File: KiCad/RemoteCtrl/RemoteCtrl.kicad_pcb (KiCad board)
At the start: 2 copper layers, 91 parts, among them J1 UI, SW1 MX1A-E1NW, SW2 MX1A-E1NW, SW3 MX1A-E1NW, SW4 MX1A-E1NW, SW5 MX1A-E1NW, SW6 MX1A-E1NW, SW7 MX1A-E1NW, SW8 MX1A-E1NW, U1 74LVC1G17, U2 74LVC1G17, U3 74LVC1G17, U4 74LVC1G17, U5 74LVC1G17, U6 74LVC1G17, U7 74LVC1G17, U8 74LVC1G17

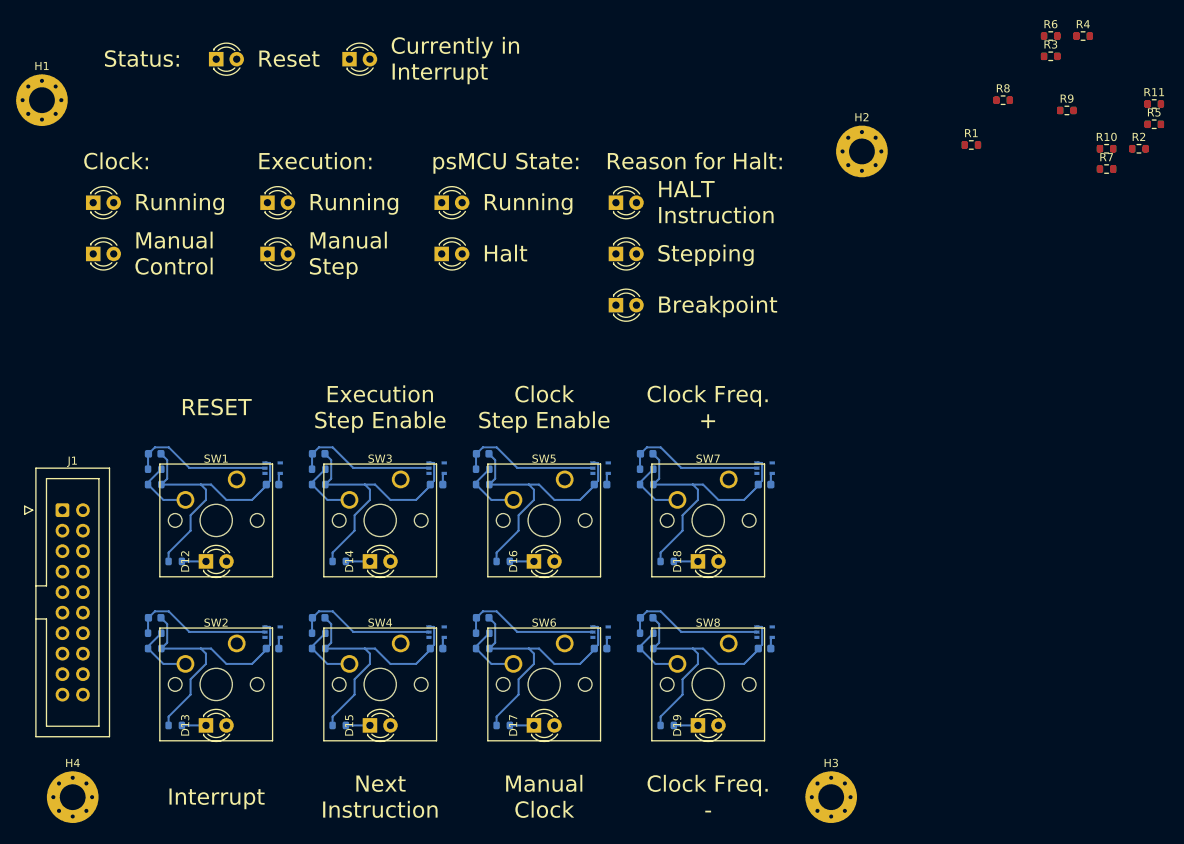
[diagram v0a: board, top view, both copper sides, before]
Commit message: Rough layout of Remote finished.
    Did not do connector yet, in case that changes with
    psMCU layout.
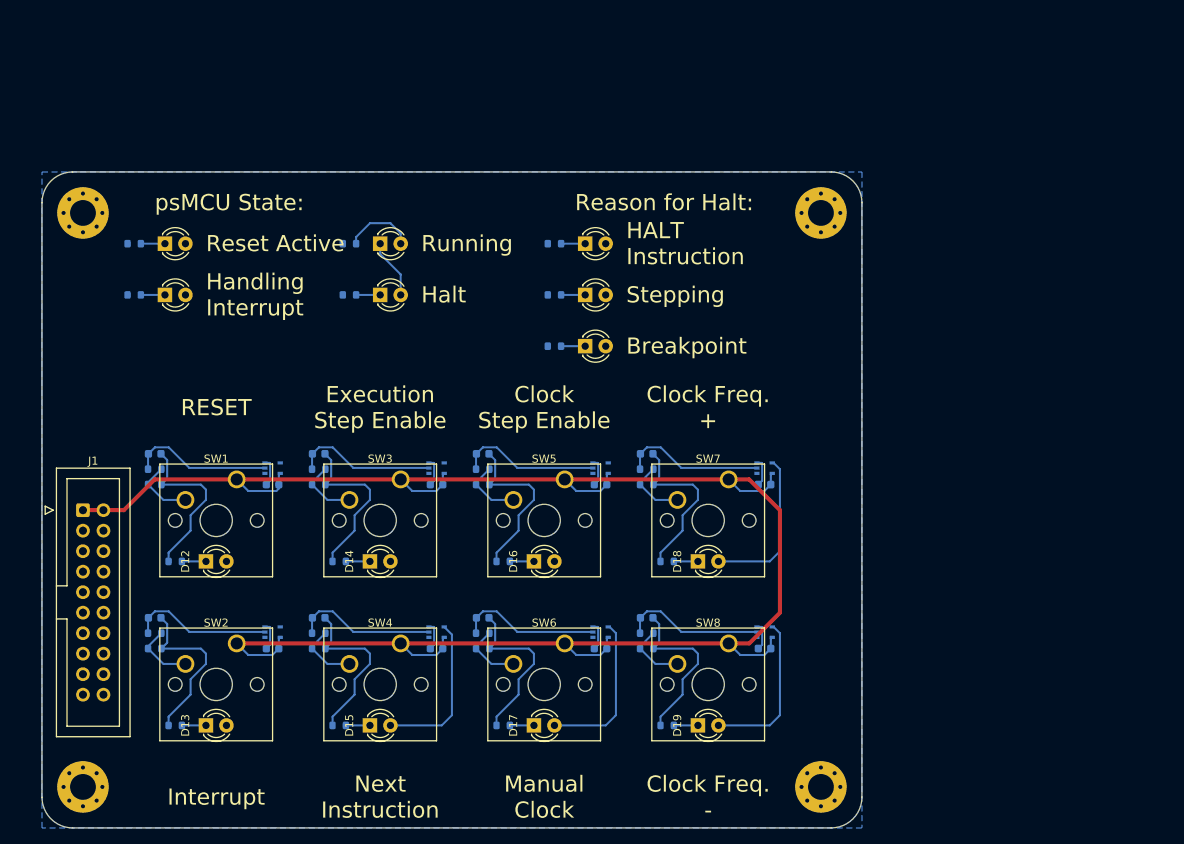
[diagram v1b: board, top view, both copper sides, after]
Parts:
- removed D3, D4, D5, D6: LED, LED_THT:LED_D3.0mm
- removed R3, R4, R5, R6: rled, Resistor_SMD:R_0603_1608Metric
- R1, R10, R11, R2, R7, R8, R9: moved to B.Cu
- moved R2 125.8 mm to (104.1, 43.2), turned to 180 degrees
- moved R1 104.4 mm to (104.1, 36.8), turned to 180 degrees
- moved R7 95.1 mm to (130.8, 43.2), turned to 180 degrees
- moved R8 82.9 mm to (130.8, 36.8), turned to 180 degrees
- moved R11 80.1 mm to (156.2, 49.5), turned to 180 degrees
- moved R10 70.8 mm to (156.2, 43.2), turned to 180 degrees
- moved R9 65.6 mm to (156.2, 36.8), turned to 180 degrees
- moved D2 37.1 mm to (108.0, 43.2)
- moved D1 23.7 mm to (108.0, 36.8)
- moved H1 14.9 mm to (97.8, 33.0)
- moved H2 9.16 mm to (189.2, 33.0)
- moved D7 9.16 mm to (134.6, 43.2)
- moved D8 9.16 mm to (134.6, 36.8)
- moved D10 6.35 mm to (160.0, 43.2)
- moved D11 6.35 mm to (160.0, 49.5)
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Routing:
- net +5V: track 11.7 -> 232.2 mm
- net GND: track 274.3 -> 196.1 mm
- net /BTN_INC_CLK_F: track 0.00 -> 19.6 mm
- net /BTN_DEC_CLK_F: track 0.00 -> 19.6 mm
- net /BTN_CLK_STEP: track 0.00 -> 19.6 mm
- net /BTN_INST_STEP: track 0.00 -> 19.5 mm
- net Net-(D8-Pad2): track 0.00 -> 8.86 mm
- net /LED_Halted: track 0.00 -> 7.40 mm
- net Net-(D9-Pad1): track 0.00 -> 2.99 mm
- net Net-(D7-Pad1): track 0.00 -> 2.99 mm
- net Net-(D11-Pad1): track 0.00 -> 2.99 mm
- net Net-(D10-Pad1): track 0.00 -> 2.99 mm
- net Net-(D2-Pad1): track 0.00 -> 2.98 mm
- net Net-(D1-Pad1): track 0.00 -> 2.98 mm
- added copper zone on B.Cu, net GND
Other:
- board outline added: 101.6 x 81.3 mm
- board text added: "Handling Interrupt"
- board text added: "Reset Active"
- board text removed: "Clock:"
- board text removed: "Currently in Interrupt"
- board text removed: "Execution:"
- board text removed: "Manual Control"
- board text removed: "Manual Step"
- board text removed: "Reset"
- board text removed: "Status:"

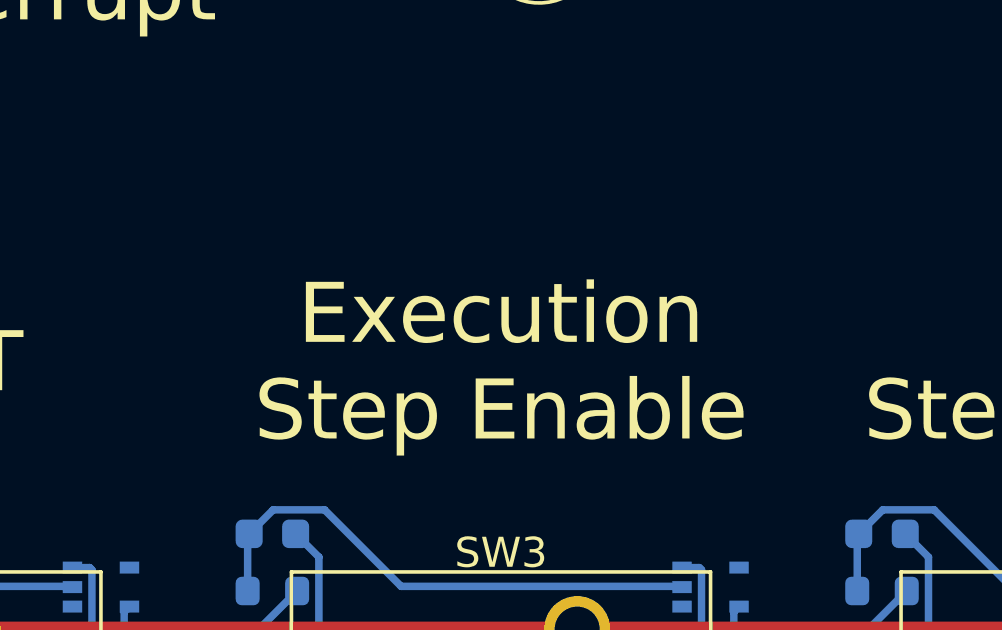
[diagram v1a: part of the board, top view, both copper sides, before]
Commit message: Worked on side-pcbs
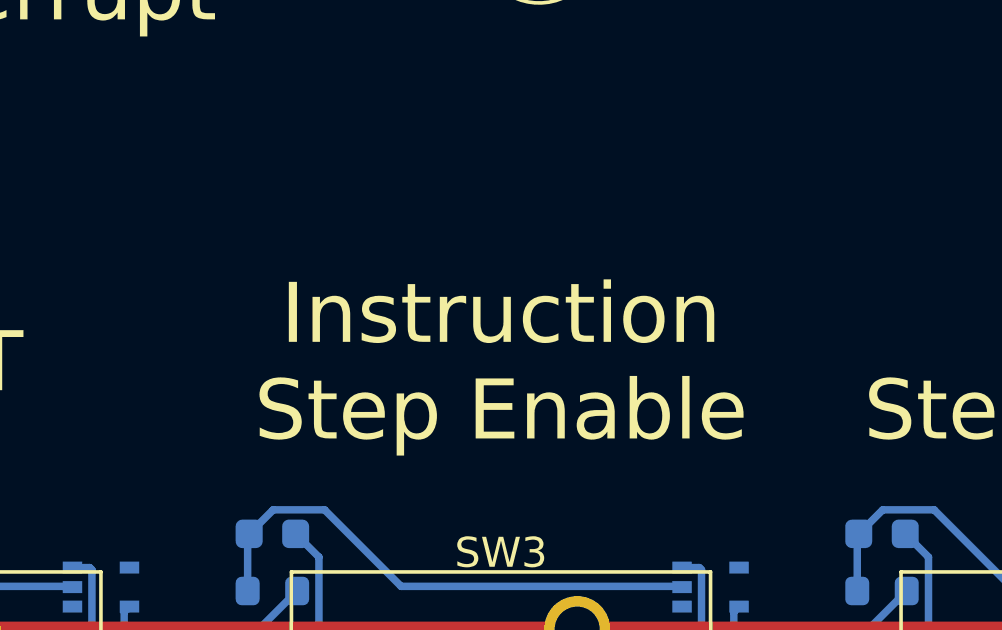
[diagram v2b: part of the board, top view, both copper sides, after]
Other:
- board text added: "Instruction Step Enable"
- board text removed: "Execution Step Enable"

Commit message: First draft Remote Control
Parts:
- moved J1 23.0 mm to (100.3, 92.7), turned to 180 degrees
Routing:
- net /LED_Halted_Inst: track 0.00 -> 109.2 mm, vias 0 -> 1
- net /BTN_INC_CLK_F: track 19.6 -> 124.6 mm, vias 0 -> 5
- net /LED_Halted_Step: track 0.00 -> 100.6 mm, vias 0 -> 1
- net /BTN_DEC_CLK_F: track 19.6 -> 108.3 mm
- net /LED_Halted_Bkpt: track 0.00 -> 88.0 mm, vias 0 -> 1
- net /BTN_CLK_STEP_EN: track 0.00 -> 82.8 mm, vias 0 -> 1
- net /LED_CLK_STEP_EN: track 0.00 -> 76.9 mm, vias 0 -> 5
- net /LED_INT_Active: track 0.00 -> 74.3 mm, vias 0 -> 4
- net /BTN_CLK_STEP: track 19.6 -> 90.2 mm, vias 0 -> 1
- net /LED_Halted: track 7.40 -> 74.6 mm, vias 0 -> 1
- net /RESET: track 0.00 -> 65.9 mm, vias 0 -> 3
- net /BTN_INST_STEP_EN: track 0.00 -> 62.5 mm, vias 0 -> 1
- net /LED_INST_STEP_EN: track 0.00 -> 61.0 mm, vias 0 -> 5
- net /BTN_INST_STEP: track 19.5 -> 76.9 mm, vias 0 -> 1
- net /BTN_RESET: track 0.00 -> 43.2 mm, vias 0 -> 1
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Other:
- board text added: "v0.1"
